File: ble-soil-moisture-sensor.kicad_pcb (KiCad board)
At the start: 2 copper layers, 170 x 18 mm, 31 parts, among them P1 CONN_02X03, Q1 Q_NMOS_GSD, Q2 Q_PMOS_GSD, Q3 Q_PMOS_GSD, U1 BGM111, U2 TPS78225

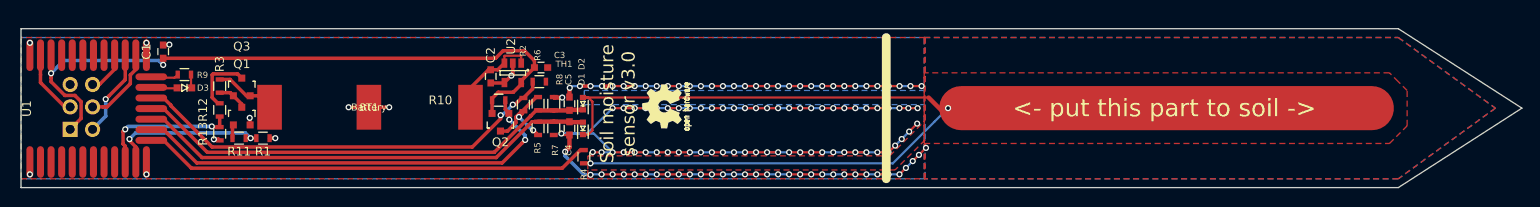
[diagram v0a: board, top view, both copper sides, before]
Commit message: Add some fogotten schematics and pcb changes. Add BOM and firmware
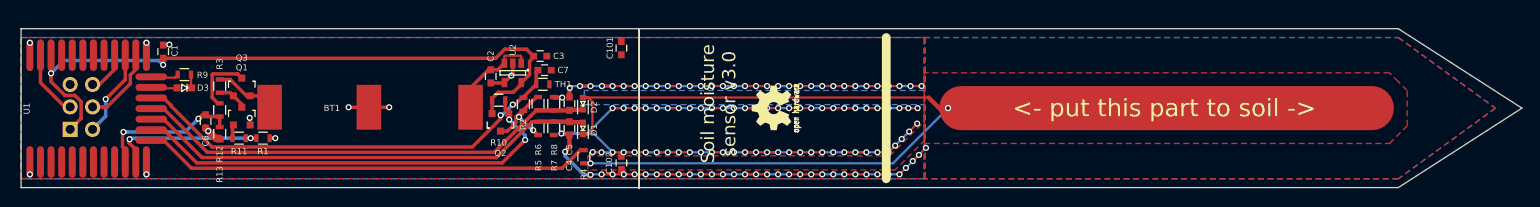
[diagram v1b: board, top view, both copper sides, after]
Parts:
- added C101: C_0603, Capacitors_SMD:C_0603, F.Cu at (148.0, 84.2)
- added C102: C_0603, Capacitors_SMD:C_0603, F.Cu at (148.0, 97.2)
- added C6: 1n, Capacitors_SMD:C_0603, F.Cu at (100.9, 92.5)
- added C7: 1n, Capacitors_SMD:C_0603, F.Cu at (139.3, 86.7)
- moved G*** 12.4 mm to (165.0, 91.0)
- moved G*** 11.0 mm to (210.0, 90.0)
- moved C3 1.30 mm to (138.8, 85.1)
- moved TH1 0.50 mm to (139.1, 88.3)
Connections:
- C4 pad 1: /SENSE_HIGH -> /SENSE_LOW
- C5 pad 1: /SENSE_LOW -> /SENSE_HIGH
- D1 pad 1: /SENSE_HIGH -> /SENSE_LOW
- D2 pad 2: /SENSE_LOW -> /SENSE_HIGH
- R5 pad 1: /SENSE_HIGH -> /SENSE_LOW
- R6 pad 1: /SENSE_LOW -> /SENSE_HIGH
- R7 pad 2: /SENSE_HIGH -> /SENSE_LOW
- R8 pad 2: /SENSE_LOW -> /SENSE_HIGH
- U1 pad 15: /SENSE_HIGH -> /SENSE_LOW
- U1 pad 16: /SENSE_LOW -> /SENSE_HIGH
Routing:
- net GND: track 206.9 -> 209.0 mm
- net /THERMISTOR: track 49.5 -> 51.0 mm
- net /BATTERY_SENSE: track 16.0 -> 16.6 mm
